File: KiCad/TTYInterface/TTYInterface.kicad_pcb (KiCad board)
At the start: 2 copper layers, 200 x 100 mm, 10 parts, among them J1 CONN_02X10, J2 DB25_MALE_MountingHoles, U1 MAX3232

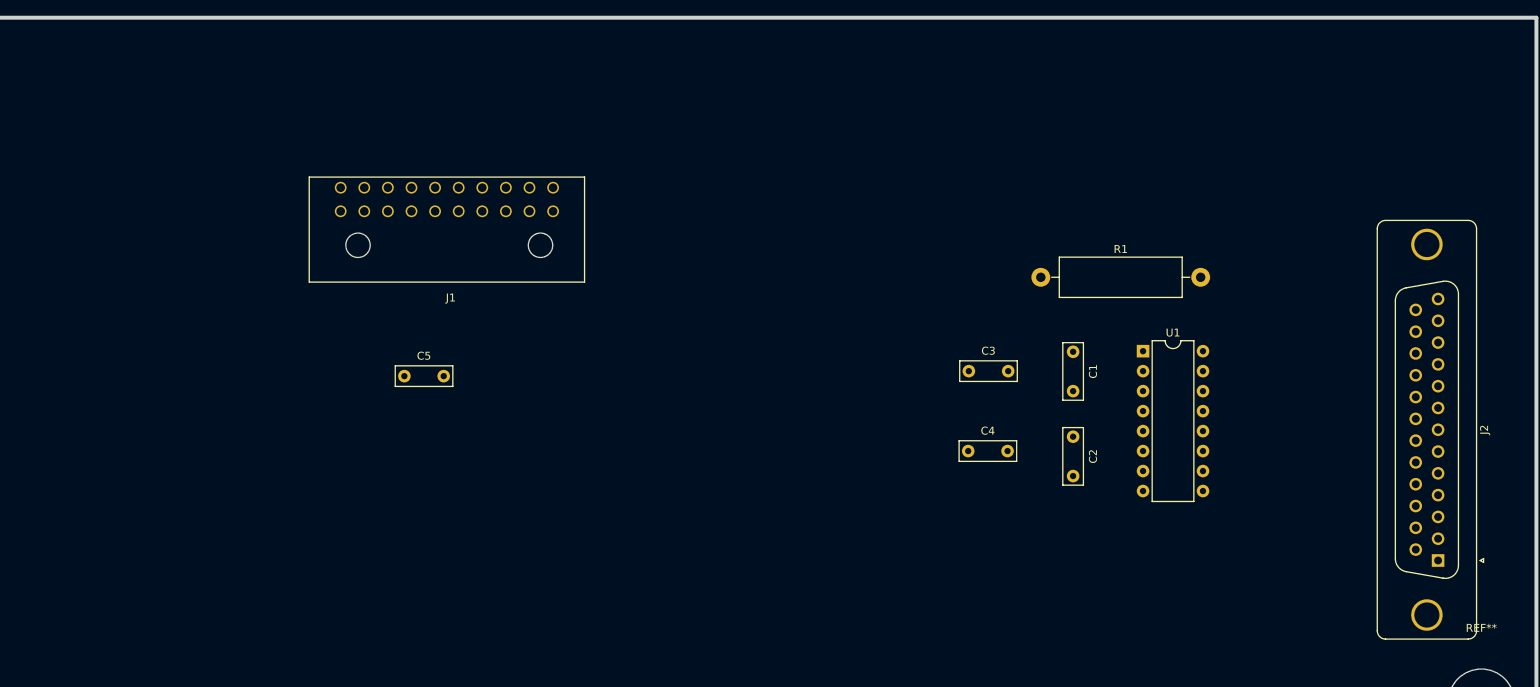
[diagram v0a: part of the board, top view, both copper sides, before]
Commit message: Update CPU and TTY Interface board
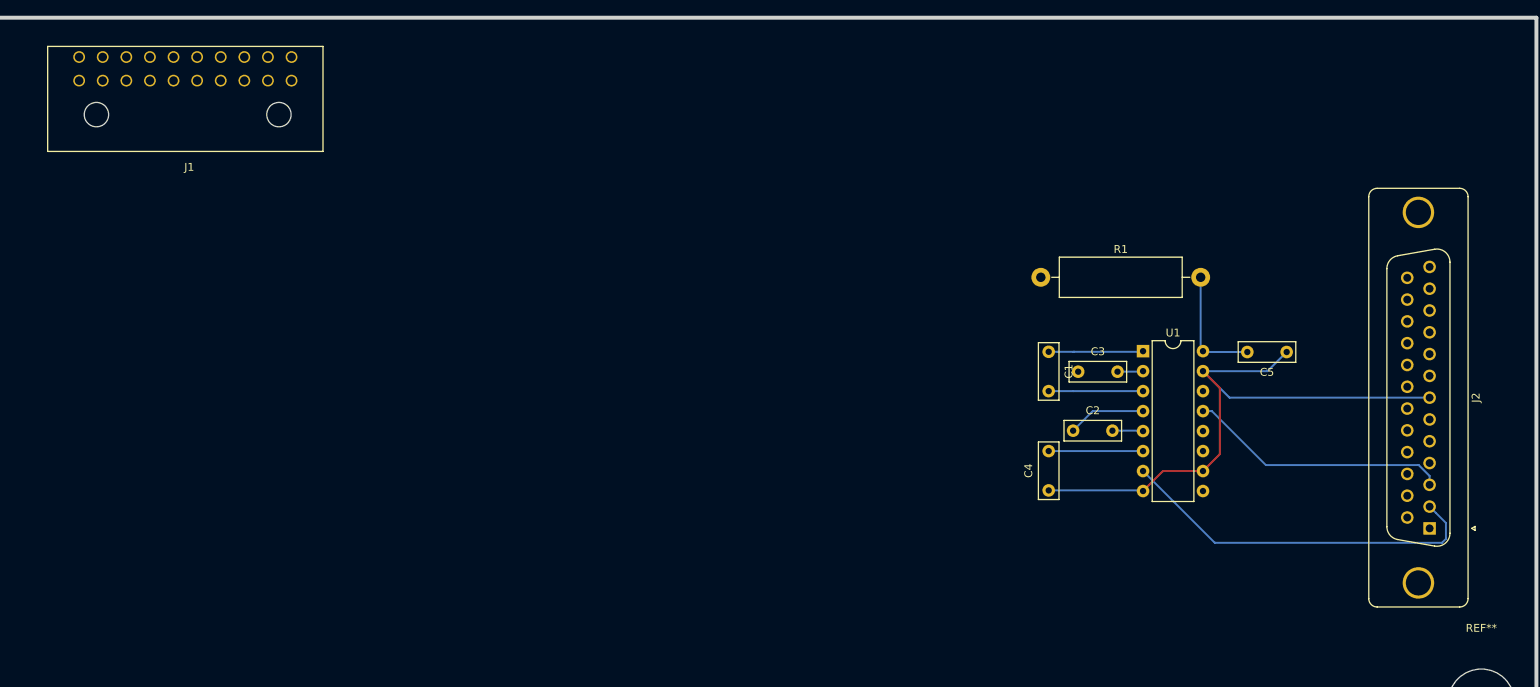
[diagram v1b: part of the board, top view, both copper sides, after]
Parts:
- moved C5 112.2 mm to (232.2, 72.5), turned to 180 degrees
- moved J1 37.2 mm to (105.8, 38.0)
- moved C3 13.9 mm to (205.8, 75.0)
- moved C4 11.4 mm to (202.0, 90.1), turned to 90 degrees
- moved J2 4.22 mm to (250.4, 94.9)
- moved C1 3.10 mm to (202.0, 72.5)
- moved C2 0.77 mm to (205.1, 82.5), turned to 0 degrees
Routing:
- net 0V: track 0.00 -> 77.0 mm
- net Net-(J2-Pad2): track 0.00 -> 47.5 mm
- net Net-(J2-Pad3): track 0.00 -> 33.3 mm
- net Net-(C5-Pad2): track 0.00 -> 15.2 mm
- net Net-(C1-Pad1): track 0.00 -> 12.2 mm
- net Net-(C4-Pad2): track 0.00 -> 12.0 mm
- net Net-(C1-Pad2): track 0.00 -> 12.0 mm
- net Net-(C2-Pad1): track 0.00 -> 9.92 mm
- net Net-(C2-Pad2): track 0.00 -> 3.91 mm
- net Net-(C3-Pad2): track 0.00 -> 3.27 mm

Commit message: Update to the PCBs
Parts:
- removed the REF** at (257.0, 117.0)
- added REF**: MountingHole_3.5mm_Pad, Mounting_Holes:MountingHole_3.5mm_Pad, F.Cu at (141.0, 124.0)
- added REF**: MountingHole_3.5mm_Pad, Mounting_Holes:MountingHole_3.5mm_Pad, F.Cu at (40.0, 124.0)
- added REF**: MountingHole_3.5mm_Pad, Mounting_Holes:MountingHole_3.5mm_Pad, F.Cu at (267.0, 80.0)
- added REF**: MountingHole_3.5mm_Pad, Mounting_Holes:MountingHole_3.5mm_Pad, F.Cu at (28.0, 36.0)
- added REF**: MountingHole_3.5mm_Pad, Mounting_Holes:MountingHole_3.5mm_Pad, F.Cu at (113.0, 36.0)
- added REF**: MountingHole_8.4mm_M8, Mounting_Holes:MountingHole_8.4mm_M8, F.Cu at (267.0, 42.0)
- added REF**: MountingHole_8.4mm_M8, Mounting_Holes:MountingHole_8.4mm_M8, F.Cu at (267.0, 118.0)
- J1: footprint Connectors_Molex:Molex_Microfit3_Header_02x10_Angled_43045-200x -> Connectors_JST:B20-J11DK_2x10_Pitch2.54mm
- moved J1 20.8 mm to (85.0, 38.0), turned to 180 degrees
- moved C1 5.59 mm to (207.5, 73.5)
- moved C2 5.59 mm to (210.6, 83.5)
- moved C3 5.59 mm to (211.2, 76.0)
- moved C4 5.59 mm to (207.5, 91.1)
- moved C5 5.59 mm to (237.8, 73.5)
- moved J2 5.59 mm to (255.9, 95.9)
- moved R1 5.59 mm to (206.5, 64.0)
- moved U1 5.59 mm to (219.5, 73.4)
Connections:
- J1 pad 1: (no net) -> Net-(J1-Pad1)
- J1 pad 10: (no net) -> Net-(J1-Pad10)
- J1 pad 11: (no net) -> Net-(J1-Pad11)
- J1 pad 12: (no net) -> Net-(J1-Pad12)
- J1 pad 13: (no net) -> Net-(J1-Pad13)
- J1 pad 14: (no net) -> Net-(J1-Pad14)
- J1 pad 16: (no net) -> Net-(J1-Pad16)
- J1 pad 18: (no net) -> Net-(J1-Pad18)
- J1 pad 2: (no net) -> Net-(J1-Pad2)
- J1 pad 20: (no net) -> Net-(J1-Pad20)
- J1 pad 3: (no net) -> Net-(J1-Pad3)
- J1 pad 4: (no net) -> Net-(J1-Pad4)
- J1 pad 5: (no net) -> Net-(J1-Pad5)
- J1 pad 6: (no net) -> Net-(J1-Pad6)
- J1 pad 8: (no net) -> Net-(J1-Pad8)
- J2 pad 0: Net-(J2-Pad0) -> 0V
- J2 pad 1: (no net) -> Net-(J2-Pad1)
- J2 pad 10: (no net) -> Net-(J2-Pad10)
- J2 pad 11: (no net) -> Net-(J2-Pad11)
- J2 pad 12: (no net) -> Net-(J2-Pad12)
- J2 pad 13: (no net) -> Net-(J2-Pad13)
- J2 pad 14: (no net) -> Net-(J2-Pad14)
- J2 pad 15: (no net) -> Net-(J2-Pad15)
- J2 pad 16: (no net) -> Net-(J2-Pad16)
- J2 pad 17: (no net) -> Net-(J2-Pad17)
- J2 pad 18: (no net) -> Net-(J2-Pad18)
- J2 pad 19: (no net) -> Net-(J2-Pad19)
- J2 pad 20: (no net) -> Net-(J2-Pad20)
- J2 pad 21: (no net) -> Net-(J2-Pad21)
- J2 pad 22: (no net) -> Net-(J2-Pad22)
- J2 pad 23: (no net) -> Net-(J2-Pad23)
- J2 pad 24: (no net) -> Net-(J2-Pad24)
- J2 pad 25: (no net) -> Net-(J2-Pad25)
- J2 pad 4: (no net) -> Net-(J2-Pad4)
- J2 pad 5: (no net) -> Net-(J2-Pad5)
- J2 pad 6: (no net) -> Net-(J2-Pad6)
- J2 pad 8: (no net) -> Net-(J2-Pad8)
- J2 pad 9: (no net) -> Net-(J2-Pad9)
- U1 pad 14: (no net) -> Net-(U1-Pad14)
- U1 pad 9: (no net) -> Net-(U1-Pad9)
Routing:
- net 0V: track 77.0 -> 312.3 mm
- net Net-(J1-Pad19): track 0.00 -> 181.8 mm
- net Net-(J1-Pad17): track 0.00 -> 178.6 mm
- net +5V: track 0.00 -> 138.9 mm
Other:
- board size 200 x 100 mm -> 255 x 100 mm

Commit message: Update the TTY PCB
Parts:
- added REF**: MountingHole_5.3mm_M5, Mounting_Holes:MountingHole_5.3mm_M5, F.Cu at (170.0, 80.0)
- J1: footprint Connectors_JST:B20-J11DK_2x10_Pitch2.54mm -> Pin_Headers:Pin_Header_Angled_2x10_Pitch2.54mm; moved to B.Cu
- J2: footprint Elliott:DSUB-25_Female_Vertical_Pitch2.77x2.84mm_MountingHoles -> TTY:DSUB-25_Female_Vertical_Pitch2.77x2.84mm_MountingHoles
- moved J1 11.1 mm to (93.6, 45.0), turned to 90 degrees
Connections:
- U1 pad 14: Net-(U1-Pad14) -> Net-(J2-Pad2)
- U1 pad 7: Net-(J2-Pad2) -> Net-(U1-Pad7)
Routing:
- net Net-(J2-Pad3): track 33.3 -> 54.5 mm
- net Net-(J1-Pad19): track 181.8 -> 195.4 mm
- net +5V: track 138.9 -> 128.4 mm
- net 0V: track 312.3 -> 302.2 mm
- net Net-(J1-Pad17): track 178.6 -> 184.7 mm
- net Net-(J2-Pad2): track 47.5 -> 48.5 mm
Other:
- net class Default: trace_width 0.25 -> 0.4

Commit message: Improvements to PCBs and footprints
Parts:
- moved J1 9.03 mm to (84.6, 45.7)
- moved REF** 1.00 mm to (112.0, 36.0)
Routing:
- net 0V: track 302.2 -> 311.3 mm
- net Net-(J1-Pad19): track 195.4 -> 204.1 mm
- net Net-(J1-Pad17): track 184.7 -> 193.4 mm
- net +5V: track 128.4 -> 137.1 mm
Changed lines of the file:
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@@
   (general
     (links 23)
-    (no_connects 0)
+    (no_connects 1)
     (area 18.085714 29.749999 276.914286 130.250001)
     (thickness 1.6)
     (drawings 4)
-    (tracks 69)
+    (tracks 72)
     (zones 0)
     (modules 17)
@@
     (mod_text_size 1 1)
     (mod_text_width 0.15)
-    (pad_size 5.3 5.3)
-    (pad_drill 5.3)
+    (pad_size 7 7)
+    (pad_drill 4)
     (pad_to_mask_clearance 0)
     (aux_axis_origin 0 0)
@@
     (fp_circle (center 0 0) (end 3.5 0) (layer Cmts.User) (width 0.15))
     (fp_circle (center 0 0) (end 3.75 0) (layer F.CrtYd) (width 0.05))
-    (pad 1 thru_hole circle (at 0 0) (size 7 7) (drill 3.5) (layers *.Cu *.Mask))
+    (pad 1 thru_hole circle (at 0 0) (size 7 7) (drill 4) (layers *.Cu *.Mask))
   )
   (module Mounting_Holes:MountingHole_3.5mm_Pad (layer F.Cu)
@@
     (fp_circle (center 0 0) (end 3.5 0) (layer Cmts.User) (width 0.15))
     (fp_circle (center 0 0) (end 3.75 0) (layer F.CrtYd) (width 0.05))
-    (pad 1 thru_hole circle (at 0 0) (size 7 7) (drill 3.5) (layers *.Cu *.Mask))
+    (pad 1 thru_hole circle (at -1 0) (size 7 7) (drill 4) (layers *.Cu *.Mask))
   )
   (module Mounting_Holes:MountingHole_3.5mm_Pad (layer F.Cu)
@@
     (fp_circle (center 0 0) (end 3.5 0) (layer Cmts.User) (width 0.15))
     (fp_circle (center 0 0) (end 3.75 0) (layer F.CrtYd) (width 0.05))
-    (pad 1 thru_hole circle (at 0 0) (size 7 7) (drill 3.5) (layers *.Cu *.Mask))
+    (pad 1 thru_hole circle (at 0 0) (size 7 7) (drill 4) (layers *.Cu *.Mask))
   )
   (module Mounting_Holes:MountingHole_3.5mm_Pad (layer F.Cu)
@@
     (fp_circle (center 0 0) (end 3.5 0) (layer Cmts.User) (width 0.15))
     (fp_circle (center 0 0) (end 3.75 0) (layer F.CrtYd) (width 0.05))
-    (pad 1 thru_hole circle (at 0 0) (size 7 7) (drill 3.5) (layers *.Cu *.Mask))
+    (pad 1 thru_hole circle (at 0 0) (size 7 7) (drill 4) (layers *.Cu *.Mask))
   )
   (module Mounting_Holes:MountingHole_3.5mm_Pad (layer F.Cu)
-    (at 113 36)
+    (at 112 36)
     (descr "Mounting Hole 3.5mm")
     (tags "mounting hole 3.5mm")
@@
   )
   (module Pin_Headers:Pin_Header_Angled_2x10_Pitch2.54mm (layer B.Cu)
-    (at 93.58 45 90)
+    (at 84.58 45.7 90)
     (descr "Through hole angled pin header, 2x10, 2.54mm pitch, 6mm pin length, double rows")
     (tags "Through hole angled pin header THT 2x10 2.54mm double row")
@@
   (segment (start 215.605 83.5) (end 219.445 83.5) (width 0.4) (layer B.Cu) (net 4) (status 30))
   (segment (start 219.445 83.5) (end 219.495 83.55) (width 0.25) (layer B.Cu) (net 4) (status 30))
-  (segment (start 211.25 76) (end 216.75 70.5) (width 0.4) (layer F.Cu) (net 5))
+  (segment (start 66.8 45.7) (end 69.6 48.5) (width 0.4) (layer B.Cu) (net 5))
+  (segment (start 69.6 48.5) (end 72.84811 48.5) (width 0.4) (layer B.Cu) (net 5))
+  (segment (start 72.84811 48.5) (end 74.42 46.92811) (width 0.4) (layer B.Cu) (net 5))
+  (segment (start 74.42 46.92811) (end 74.42 46.902081) (width 0.4) (layer B.Cu) (net 5))
+  (segment (start 74.427803 45.692196) (end 74.526476 45.790869) (width 0.4) (layer B.Cu) (net 5) (status 30))
+  (segment (start 74.072002 46.047997) (end 74.374521 46.350516) (width 0.4) (layer B.Cu) (net 5) (status 30))
+  (segment (start 174 66.25) (end 93.767919 66.25) (width 0.4) (layer B.Cu) (net 5))
+  (segment (start 74.42 45.7) (end 74.42 46.902081) (width 0.4) (layer B.Cu) (net 5) (status 10))
+  (segment (start 74.42 46.902081) (end 93.767919 66.25) (width 0.4) (layer B.Cu) (net 5))
+  (segment (start 211.25 76) (end 216.75 70.5) (width 0.4) (layer F.Cu) (net 5) (status 10))
   (segment (start 216.75 70.5) (end 221.685 70.5) (width 0.4) (layer F.Cu) (net 5))
   (segment (start 221.685 70.5) (end 225.989999 74.804999) (width 0.4) (layer F.Cu) (net 5))
-  (segment (start 83.42 45) (end 82.570001 45.849999) (width 0.4) (layer B.Cu) (net 5))
-  (segment (start 82.570001 45.849999) (end 82.570001 46.179999) (width 0.4) (layer B.Cu) (net 5))
-  (segment (start 82.570001 46.179999) (end 80.75 48) (width 0.4) (layer B.Cu) (net 5))
-  (segment (start 80.75 48) (end 78.8 48) (width 0.4) (layer B.Cu) (net 5))
-  (segment (start 78.8 48) (end 76.649999 45.849999) (width 0.4) (layer B.Cu) (net 5))
-  (segment (start 76.649999 45.849999) (end 75.8 45) (width 0.4) (layer B.Cu) (net 5))
-  (segment (start 174 66.25) (end 104.67 66.25) (width 0.4) (layer B.Cu) (net 5))
-  (segment (start 104.67 66.25) (end 83.42 45) (width 0.4) (layer B.Cu) (net 5))
   (segment (start 182.950001 75.200001) (end 174 66.25) (width 0.4) (layer B.Cu) (net 5))
-  (segment (start 211.25 76) (end 210.450001 75.200001) (width 0.4) (layer B.Cu) (net 5))
+  (segment (start 211.25 76) (end 210.450001 75.200001) (width 0.4) (layer B.Cu) (net 5) (status 10))
   (segment (start 210.450001 75.200001) (end 182.950001 75.200001) (width 0.4) (layer B.Cu) (net 5))
   (segment (start 237.75 73.5) (end 254.5 56.75) (width 0.4) (layer F.Cu) (net 5) (status 30))
@@
   (segment (start 207.5 91.09) (end 219.415 91.09) (width 0.4) (layer B.Cu) (net 5) (status 30))
   (segment (start 219.415 91.09) (end 219.495 91.17) (width 0.25) (layer B.Cu) (net 5) (status 30))
-  (segment (start 216.25 76) (end 219.425 76) (width 0.4) (layer B.Cu) (net 6))
-  (segment (start 219.425 76) (end 219.495 75.93) (width 0.4) (layer B.Cu) (net 6))
+  (segment (start 216.25 76) (end 219.425 76) (width 0.4) (layer B.Cu) (net 6) (status 30))
+  (segment (start 219.425 76) (end 219.495 75.93) (width 0.4) (layer B.Cu) (net 6) (status 30))
   (segment (start 207.5 86.09) (end 219.495 86.09) (width 0.4) (layer B.Cu) (net 7) (status 30))
-  (segment (start 206.5 64) (end 104.96 64) (width 0.4) (layer B.Cu) (net 8) (status 10))
-  (segment (start 104.96 64) (end 85.96 45) (width 0.4) (layer B.Cu) (net 8) (status 20))
-  (segment (start 227.115 83.55) (end 225 85.665) (width 0.4) (layer B.Cu) (net 9) (status 10))
-  (segment (start 225 85.665) (end 225 92.75) (width 0.4) (layer B.Cu) (net 9))
-  (segment (start 225 92.75) (end 221.25 96.5) (width 0.4) (layer B.Cu) (net 9))
-  (segment (start 221.25 96.5) (end 124.76 96.5) (width 0.4) (layer B.Cu) (net 9))
-  (segment (start 124.76 96.5) (end 73.26 45) (width 0.4) (layer B.Cu) (net 9) (status 20))
-  (segment (start 70.72 45) (end 123.97 98.25) (width 0.4) (layer B.Cu) (net 10))
-  (segment (start 123.97 98.25) (end 229.5 98.25) (width 0.4) (layer B.Cu) (net 10))
+  (segment (start 76.96 45.7) (end 95.229091 63.969091) (width 0.4) (layer B.Cu) (net 8) (status 10))
+  (segment (start 95.229091 63.969091) (end 105.069091 63.969091) (width 0.4) (layer B.Cu) (net 8))
+  (segment (start 105.069091 63.969091) (end 105.1 64) (width 0.4) (layer B.Cu) (net 8))
+  (segment (start 206.5 64) (end 105.1 64) (width 0.4) (layer B.Cu) (net 8) (status 10))
+  (segment (start 64.26 45.7) (end 115.06 96.5) (width 0.4) (layer B.Cu) (net 9) (status 10))
+  (segment (start 115.06 96.5) (end 221.25 96.5) (width 0.4) (layer B.Cu) (net 9))
+  (segment (start 221.25 96.5) (end 225 92.75) (width 0.4) (layer B.Cu) (net 9))
+  (segment (start 225 92.75) (end 225 85.665) (width 0.4) (layer B.Cu) (net 9))
+  (segment (start 225 85.665) (end 227.115 83.55) (width 0.4) (layer B.Cu) (net 9) (status 20))
+  (segment (start 61.72 45.7) (end 114.27 98.25) (width 0.4) (layer B.Cu) (net 10) (status 10))
+  (segment (start 114.27 98.25) (end 229.5 98.25) (width 0.4) (layer B.Cu) (net 10))
   (segment (start 229.5 98.25) (end 231.25 96.5) (width 0.4) (layer B.Cu) (net 10))
   (segment (start 231.25 96.5) (end 231.25 90.225) (width 0.4) (layer B.Cu) (net 10))
-  (segment (start 231.25 90.225) (end 227.115 86.09) (width 0.4) (layer B.Cu) (net 10))
+  (segment (start 231.25 90.225) (end 227.115 86.09) (width 0.4) (layer B.Cu) (net 10) (status 20))
   (segment (start 227.115 78.47) (end 247.395 98.75) (width 0.4) (layer B.Cu) (net 11) (status 10))
   (segment (start 259.25 94) (end 258.4 93.15) (width 0.4) (layer B.Cu) (net 11))
